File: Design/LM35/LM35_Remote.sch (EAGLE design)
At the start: 9 parts

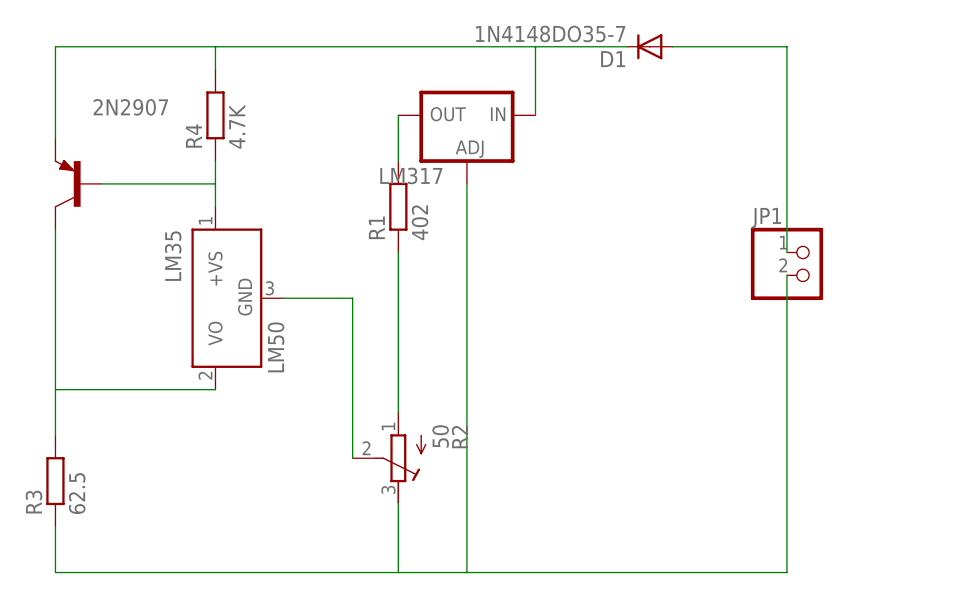
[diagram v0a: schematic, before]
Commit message: Modificado el diseno de la  placa del sensor
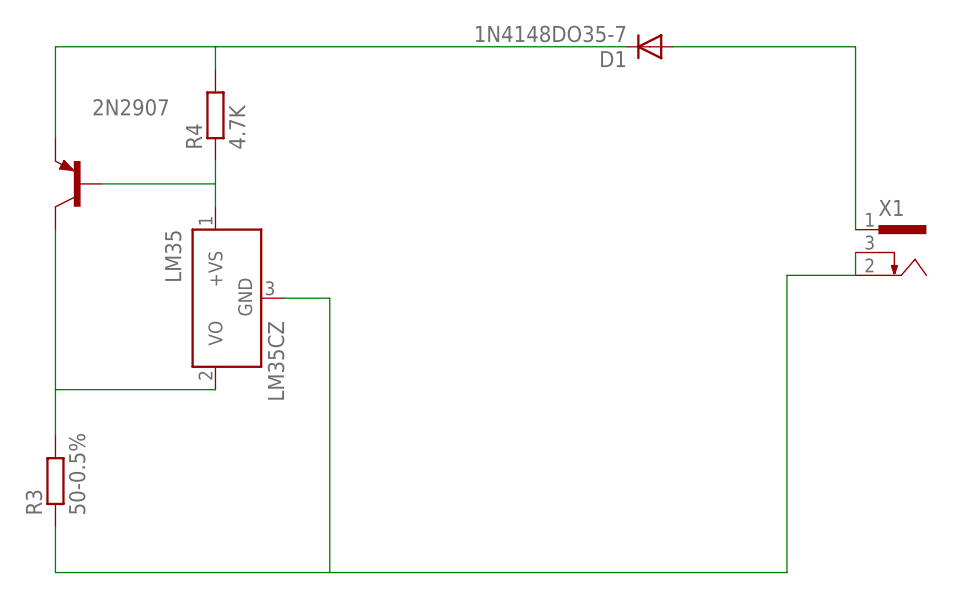
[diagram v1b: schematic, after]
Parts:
- removed JP1: (no value), pinhead:PINHD-1X2
- removed LM317: (no value), v-reg:LM317TS
- removed R1: 402, resistor:R-EU_0207_7
- removed R2: 50, resistor:R-TRIMM3296W
- added X1: (no value), con-shiua-chyuan:SCD-014A
- LM35: value LM50 -> LM35CZ; device linear:LM50 -> lm35:LM35CZ
- R3: value 62.5 -> 50-0.5%
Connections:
- removed net N$6: LM317.OUT, R1.2
- removed net N$7: LM35.GND, R2.S
- removed net N$8: D1.A, JP1.1
- net N$3: no longer LM317.IN
- net N$4: now also LM35.GND, X1.2, X1.3; no longer JP1.2, LM317.ADJ, R2.A
- net N$5: now also D1.A, X1.1; no longer R1.1, R2.E

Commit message: Ultima revision del resumen semanal
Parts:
- renumbered X1 to PLUG
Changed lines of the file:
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@@
 <part name="D1" library="diode" deviceset="1N4148" device="DO35-7"/>
 <part name="LM35" library="lm35" deviceset="LM35" device="CZ"/>
-<part name="X1" library="con-shiua-chyuan" deviceset="SCD-014A" device=""/>
+<part name="PLUG" library="con-shiua-chyuan" deviceset="SCD-014A" device=""/>
 </parts>
 <sheets>
@@
 <instance part="D1" gate="G$1" x="60.96" y="116.84" rot="R180"/>
 <instance part="LM35" gate="G$1" x="12.7" y="88.9" rot="MR270"/>
-<instance part="X1" gate="G$1" x="88.9" y="93.98"/>
+<instance part="PLUG" gate="G$1" x="88.9" y="93.98"/>
 </instances>
 <busses>
@@
 <wire x1="25.4" y1="88.9" x2="25.4" y2="58.42" width="0.1524" layer="91"/>
 <pinref part="LM35" gate="G$1" pin="GND"/>
-<pinref part="X1" gate="G$1" pin="2"/>
+<pinref part="PLUG" gate="G$1" pin="2"/>
 <wire x1="76.2" y1="91.44" x2="83.82" y2="91.44" width="0.1524" layer="91"/>
-<pinref part="X1" gate="G$1" pin="3"/>
+<pinref part="PLUG" gate="G$1" pin="3"/>
 <wire x1="83.82" y1="91.44" x2="83.82" y2="93.98" width="0.1524" layer="91"/>
 </segment>
@@
 <segment>
 <pinref part="D1" gate="G$1" pin="A"/>
-<pinref part="X1" gate="G$1" pin="1"/>
+<pinref part="PLUG" gate="G$1" pin="1"/>
 <wire x1="63.5" y1="116.84" x2="83.82" y2="116.84" width="0.1524" layer="91"/>
 <wire x1="83.82" y1="116.84" x2="83.82" y2="96.52" width="0.1524" layer="91"/>

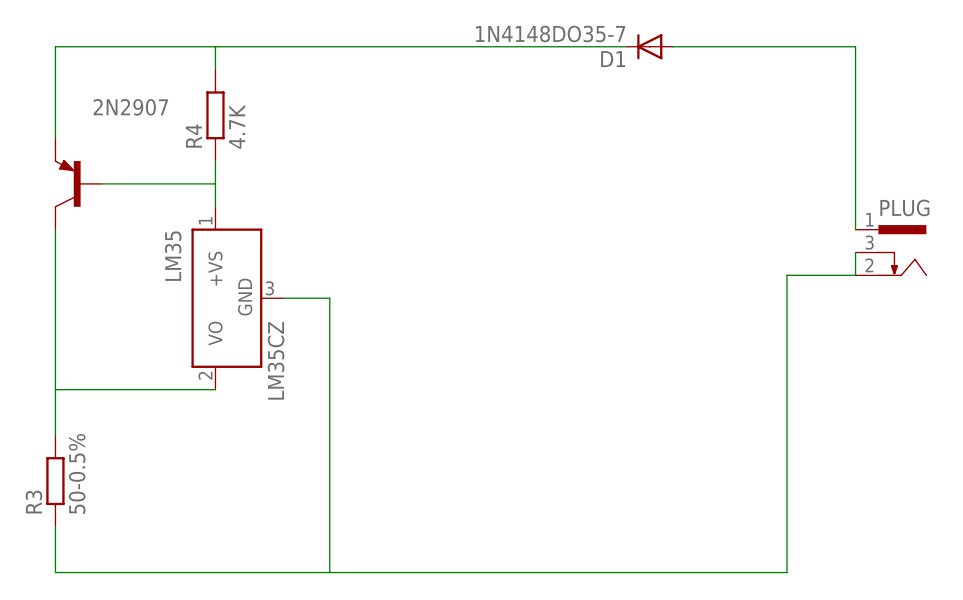
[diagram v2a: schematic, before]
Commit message: Pequeñas modificaciones en el conector jack
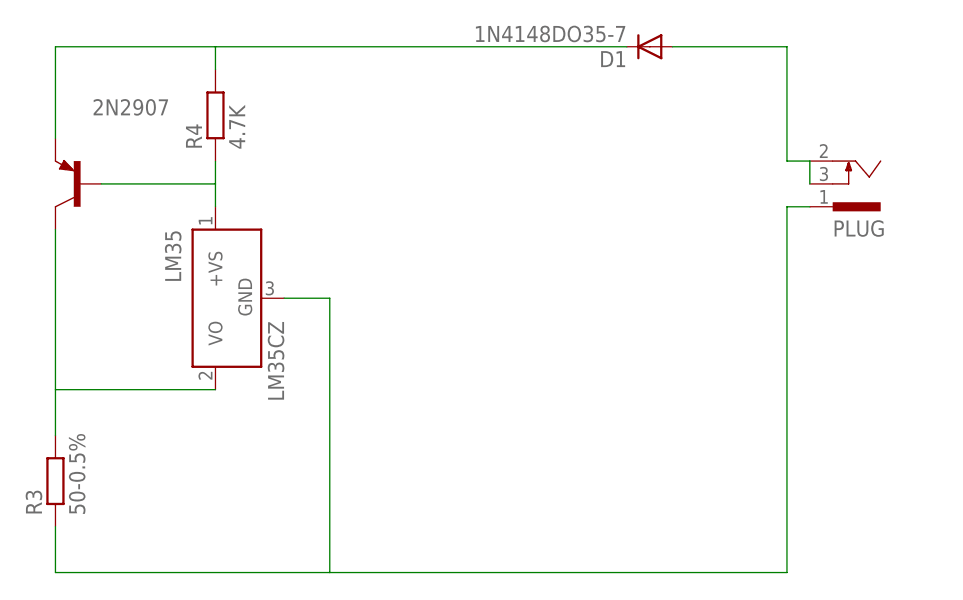
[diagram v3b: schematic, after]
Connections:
- removed net N$5: D1.A, PLUG.1
- new net N$7: D1.A, PLUG.2, PLUG.3
- net N$4: now also PLUG.1; no longer PLUG.2, PLUG.3
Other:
- moved on the sheet: PLUG
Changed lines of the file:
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@@
 <instance part="D1" gate="G$1" x="60.96" y="116.84" rot="R180"/>
 <instance part="LM35" gate="G$1" x="12.7" y="88.9" rot="MR270"/>
-<instance part="PLUG" gate="G$1" x="88.9" y="93.98"/>
+<instance part="PLUG" gate="G$1" x="83.82" y="101.6" rot="MR180"/>
 </instances>
 <busses>
@@
 <wire x1="-5.08" y1="58.42" x2="25.4" y2="58.42" width="0.1524" layer="91"/>
 <wire x1="25.4" y1="58.42" x2="76.2" y2="58.42" width="0.1524" layer="91"/>
-<wire x1="76.2" y1="58.42" x2="76.2" y2="91.44" width="0.1524" layer="91"/>
+<wire x1="76.2" y1="58.42" x2="76.2" y2="99.06" width="0.1524" layer="91"/>
 <wire x1="20.32" y1="88.9" x2="25.4" y2="88.9" width="0.1524" layer="91"/>
 <wire x1="25.4" y1="88.9" x2="25.4" y2="58.42" width="0.1524" layer="91"/>
 <pinref part="LM35" gate="G$1" pin="GND"/>
-<pinref part="PLUG" gate="G$1" pin="2"/>
-<wire x1="76.2" y1="91.44" x2="83.82" y2="91.44" width="0.1524" layer="91"/>
-<pinref part="PLUG" gate="G$1" pin="3"/>
-<wire x1="83.82" y1="91.44" x2="83.82" y2="93.98" width="0.1524" layer="91"/>
+<pinref part="PLUG" gate="G$1" pin="1"/>
+<wire x1="76.2" y1="99.06" x2="78.74" y2="99.06" width="0.1524" layer="91"/>
 </segment>
 </net>
-<net name="N$5" class="0">
+<net name="N$7" class="0">
 <segment>
+<pinref part="PLUG" gate="G$1" pin="3"/>
+<pinref part="PLUG" gate="G$1" pin="2"/>
+<wire x1="78.74" y1="104.14" x2="78.74" y2="101.6" width="0.1524" layer="91"/>
+<wire x1="78.74" y1="104.14" x2="76.2" y2="104.14" width="0.1524" layer="91"/>
+<wire x1="76.2" y1="104.14" x2="76.2" y2="116.84" width="0.1524" layer="91"/>
 <pinref part="D1" gate="G$1" pin="A"/>
-<pinref part="PLUG" gate="G$1" pin="1"/>
-<wire x1="63.5" y1="116.84" x2="83.82" y2="116.84" width="0.1524" layer="91"/>
-<wire x1="83.82" y1="116.84" x2="83.82" y2="96.52" width="0.1524" layer="91"/>
+<wire x1="76.2" y1="116.84" x2="63.5" y2="116.84" width="0.1524" layer="91"/>
 </segment>
 </net>

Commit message: Fix Doc files
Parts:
- removed 2N2907: (no value), transistor:2N2907A-PNP-TO18-EBC
- removed PLUG: (no value), con-shiua-chyuan:SCD-014A
- added 2N3906: (no value), transistor-neu-to92:2N3906-PNP-TO92-EBC
- added JP1: (no value), pinhead:PINHD-1X2
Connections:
- removed net N$4: LM35.GND, PLUG.1, R3.1
- removed net N$7: D1.A, PLUG.2, PLUG.3
- new net IN: D1.A, JP1.1
- new net OUT: JP1.2, LM35.GND, R3.1
- net N$1: now also 2N3906.B; no longer 2N2907.B
- net N$2: now also 2N3906.C; no longer 2N2907.C
- net N$3: now also 2N3906.E; no longer 2N2907.E
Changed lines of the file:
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@@
 <?xml version="1.0" encoding="utf-8"?>
 <!DOCTYPE eagle SYSTEM "eagle.dtd">
-<eagle version="7.1.0">
+<eagle version="7.2.0">
 <drawing>
 <settings>
@@
 </classes>
 <parts>
-<part name="2N2907" library="transistor" deviceset="*-PNP-" device="TO18-EBC" technology="2N2907A"/>
+<part name="2N3906" library="transistor-neu-to92" deviceset="*-PNP-" device="TO92-EBC" technology="2N3906"/>
 <part name="R3" library="resistor" deviceset="R-EU_" device="0207_7" value="50-0.5%"/>
 <part name="R4" library="resistor" deviceset="R-EU_" device="0207_7" value="4.7K"/>
 <part name="D1" library="diode" deviceset="1N4148" device="DO35-7"/>
 <part name="LM35" library="lm35" deviceset="LM35" device="CZ"/>
-<part name="PLUG" library="con-shiua-chyuan" deviceset="SCD-014A" device=""/>
+<part name="JP1" library="pinhead" deviceset="PINHD-1X2" device=""/>
 </parts>
 <sheets>
@@
 </plain>
 <instances>
-<instance part="2N2907" gate="G$1" x="-2.54" y="101.6" rot="MR0"/>
+<instance part="2N3906" gate="G$1" x="-2.54" y="101.6" rot="MR0"/>
 <instance part="R3" gate="G$1" x="-5.08" y="68.58" rot="R90"/>
 <instance part="R4" gate="G$1" x="12.7" y="109.22" rot="R90"/>
 <instance part="D1" gate="G$1" x="60.96" y="116.84" rot="R180"/>
 <instance part="LM35" gate="G$1" x="12.7" y="88.9" rot="MR270"/>
-<instance part="PLUG" gate="G$1" x="83.82" y="101.6" rot="MR180"/>
+<instance part="JP1" gate="G$1" x="86.36" y="99.06"/>
 </instances>
 <busses>
@@
 <pinref part="R4" gate="G$1" pin="1"/>
 <wire x1="12.7" y1="104.14" x2="12.7" y2="101.6" width="0.1524" layer="91"/>
-<pinref part="2N2907" gate="G$1" pin="B"/>
+<pinref part="2N3906" gate="G$1" pin="B"/>
 <wire x1="12.7" y1="101.6" x2="12.7" y2="99.06" width="0.1524" layer="91"/>
 <wire x1="0" y1="101.6" x2="12.7" y2="101.6" width="0.1524" layer="91"/>
@@
 <net name="N$2" class="0">
 <segment>
-<pinref part="2N2907" gate="G$1" pin="C"/>
+<pinref part="2N3906" gate="G$1" pin="C"/>
 <wire x1="-5.08" y1="96.52" x2="-5.08" y2="78.74" width="0.1524" layer="91"/>
 <wire x1="-5.08" y1="78.74" x2="12.7" y2="78.74" width="0.1524" layer="91"/>
@@
 <wire x1="-5.08" y1="116.84" x2="-5.08" y2="106.68" width="0.1524" layer="91"/>
 <pinref part="D1" gate="G$1" pin="C"/>
-<pinref part="2N2907" gate="G$1" pin="E"/>
+<pinref part="2N3906" gate="G$1" pin="E"/>
 </segment>
 </net>
-<net name="N$4" class="0">
+<net name="OUT" class="0">
 <segment>
 <pinref part="R3" gate="G$1" pin="1"/>
@@
 <wire x1="25.4" y1="88.9" x2="25.4" y2="58.42" width="0.1524" layer="91"/>
 <pinref part="LM35" gate="G$1" pin="GND"/>
-<pinref part="PLUG" gate="G$1" pin="1"/>
-<wire x1="76.2" y1="99.06" x2="78.74" y2="99.06" width="0.1524" layer="91"/>
+<pinref part="JP1" gate="G$1" pin="2"/>
+<wire x1="76.2" y1="99.06" x2="83.82" y2="99.06" width="0.1524" layer="91"/>
+<label x="71.12" y="58.42" size="1.778" layer="95"/>
 </segment>
 </net>
-<net name="N$7" class="0">
+<net name="IN" class="0">
 <segment>
-<pinref part="PLUG" gate="G$1" pin="3"/>
-<pinref part="PLUG" gate="G$1" pin="2"/>
 <wire x1="78.74" y1="104.14" x2="78.74" y2="101.6" width="0.1524" layer="91"/>
 <wire x1="78.74" y1="104.14" x2="76.2" y2="104.14" width="0.1524" layer="91"/>
@@
 <pinref part="D1" gate="G$1" pin="A"/>
 <wire x1="76.2" y1="116.84" x2="63.5" y2="116.84" width="0.1524" layer="91"/>
+<pinref part="JP1" gate="G$1" pin="1"/>
+<wire x1="78.74" y1="101.6" x2="83.82" y2="101.6" width="0.1524" layer="91"/>
+<label x="73.66" y="116.84" size="1.778" layer="95"/>
 </segment>
 </net>
